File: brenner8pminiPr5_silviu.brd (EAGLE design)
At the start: 82.5 x 43 mm, 39 parts, among them IC1 PIC18F2550SP, Q1 20 MHz, Q2 BC338-25, Q3 BC338-25, Q4 BC328-25, Q5 BC328-25, Q6 BF959, X2 USB-B-H

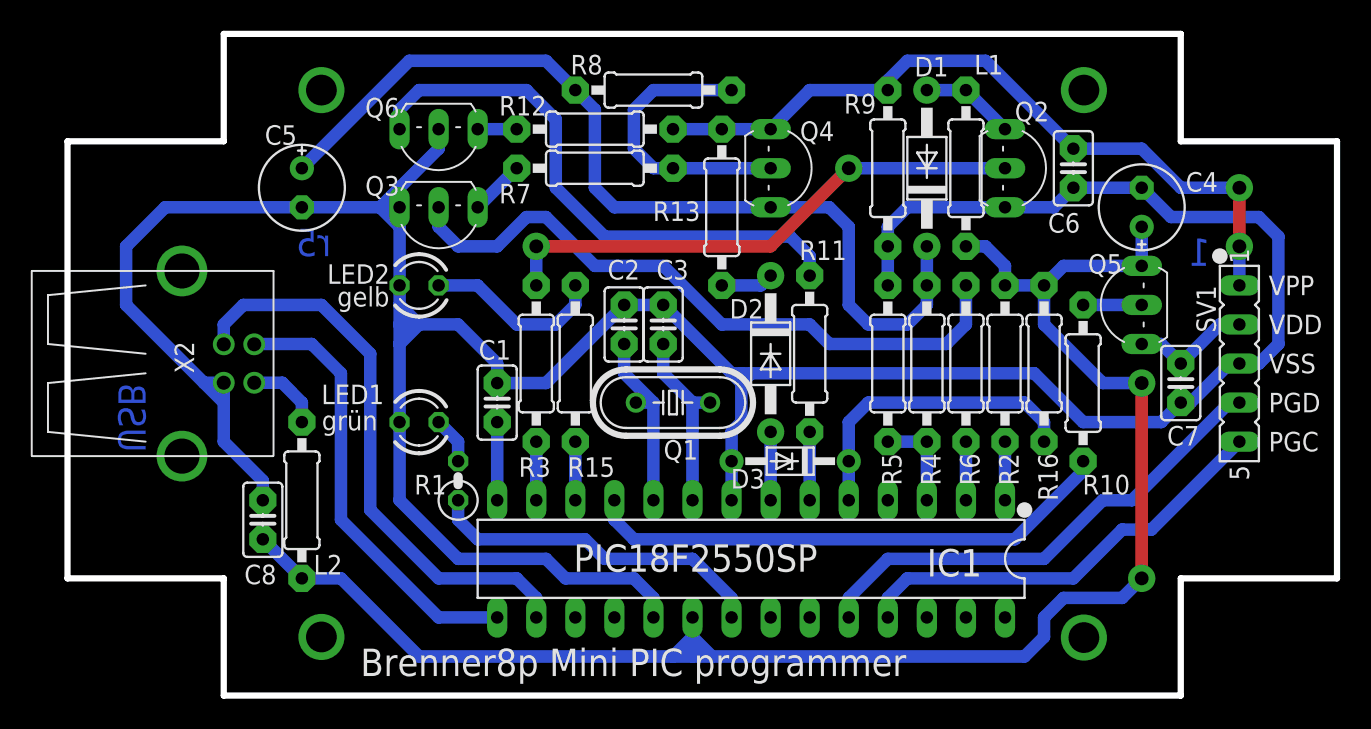
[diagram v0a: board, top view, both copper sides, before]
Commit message: Rectangular dimensions
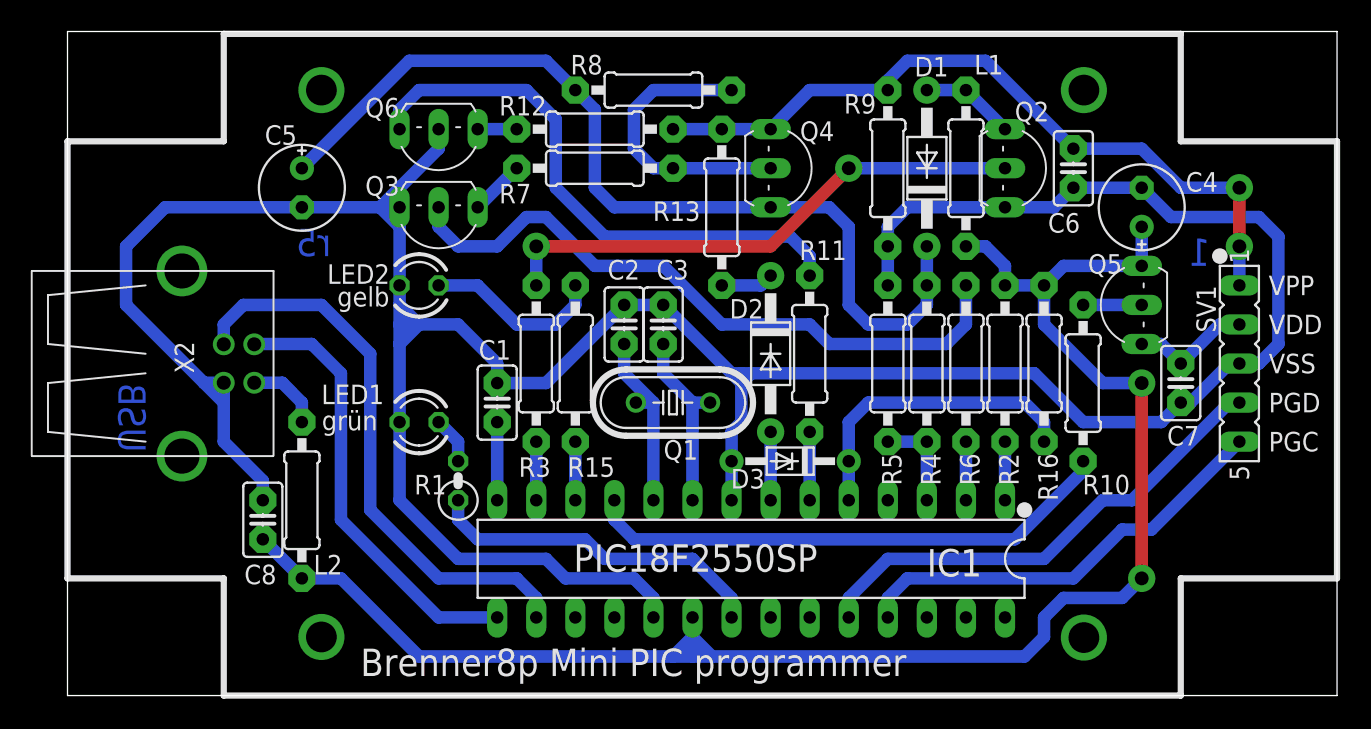
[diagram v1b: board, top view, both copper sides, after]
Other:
- board size 82.5 x 43 mm -> 82.5 x 43.2 mm
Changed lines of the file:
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@@
 <board>
 <plain>
-<wire x1="0" y1="6.35" x2="0" y2="34.77" width="0.4064" layer="20"/>
-<wire x1="10.16" y1="41.755" x2="72.39" y2="41.755" width="0.4064" layer="20"/>
-<wire x1="82.55" y1="34.77" x2="82.55" y2="6.35" width="0.4064" layer="20"/>
-<wire x1="72.39" y1="-1.27" x2="10.16" y2="-1.27" width="0.4064" layer="20"/>
-<wire x1="10.16" y1="-1.27" x2="10.16" y2="6.35" width="0.4064" layer="20"/>
-<wire x1="10.16" y1="34.77" x2="10.16" y2="41.755" width="0.4064" layer="20"/>
-<wire x1="0" y1="6.35" x2="10.16" y2="6.35" width="0.4064" layer="20"/>
-<wire x1="0" y1="34.77" x2="10.16" y2="34.77" width="0.4064" layer="20"/>
-<wire x1="72.39" y1="41.755" x2="72.39" y2="34.77" width="0.4064" layer="20"/>
-<wire x1="72.39" y1="6.35" x2="72.39" y2="-1.27" width="0.4064" layer="20"/>
-<wire x1="82.55" y1="34.77" x2="72.39" y2="34.77" width="0.4064" layer="20"/>
-<wire x1="82.55" y1="6.35" x2="72.39" y2="6.35" width="0.4064" layer="20"/>
+<wire x1="0" y1="6.35" x2="0" y2="34.77" width="0.4064" layer="21"/>
+<wire x1="10.16" y1="41.755" x2="72.39" y2="41.755" width="0.4064" layer="21"/>
+<wire x1="82.55" y1="34.77" x2="82.55" y2="6.35" width="0.4064" layer="21"/>
+<wire x1="72.39" y1="-1.27" x2="10.16" y2="-1.27" width="0.4064" layer="21"/>
+<wire x1="10.16" y1="-1.27" x2="10.16" y2="6.35" width="0.4064" layer="21"/>
+<wire x1="10.16" y1="34.77" x2="10.16" y2="41.755" width="0.4064" layer="21"/>
+<wire x1="0" y1="6.35" x2="10.16" y2="6.35" width="0.4064" layer="21"/>
+<wire x1="0" y1="34.77" x2="10.16" y2="34.77" width="0.4064" layer="21"/>
+<wire x1="72.39" y1="41.755" x2="72.39" y2="34.77" width="0.4064" layer="21"/>
+<wire x1="72.39" y1="6.35" x2="72.39" y2="-1.27" width="0.4064" layer="21"/>
+<wire x1="82.55" y1="34.77" x2="72.39" y2="34.77" width="0.4064" layer="21"/>
+<wire x1="82.55" y1="6.35" x2="72.39" y2="6.35" width="0.4064" layer="21"/>
 <text x="5.08" y="19.05" size="1.778" layer="16" font="vector" ratio="15" rot="MR270">USB</text>
 <text x="17.145" y="27.305" size="1.778" layer="16" font="vector" ratio="15" rot="MR0">r5</text>
@@
 <text x="78.105" y="17.145" size="1.27" layer="21" ratio="10">PGD</text>
 <text x="78.105" y="14.605" size="1.27" layer="21" ratio="10">PGC</text>
+<wire x1="0" y1="-1.27" x2="82.55" y2="-1.27" width="0" layer="20"/>
+<wire x1="82.55" y1="-1.27" x2="82.55" y2="41.91" width="0" layer="20"/>
+<wire x1="82.55" y1="41.91" x2="0" y2="41.91" width="0" layer="20"/>
+<wire x1="0" y1="41.91" x2="0" y2="-1.27" width="0" layer="20"/>
 </plain>
 <attributes>
